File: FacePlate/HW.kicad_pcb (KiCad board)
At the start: 2 copper layers, 8 parts, among them J1 Left, J2 Audio In, J3 Audio Out, J4 Right

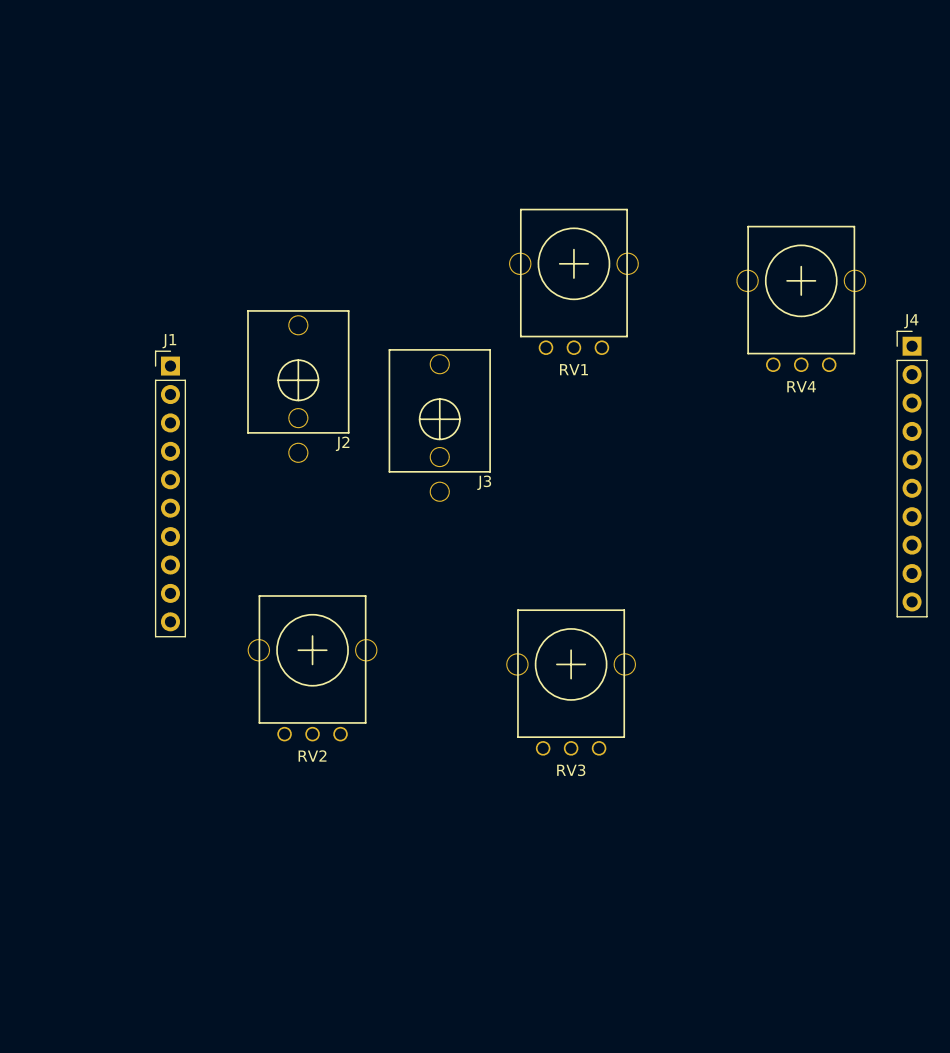
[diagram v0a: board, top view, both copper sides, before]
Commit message: Finished the IO module
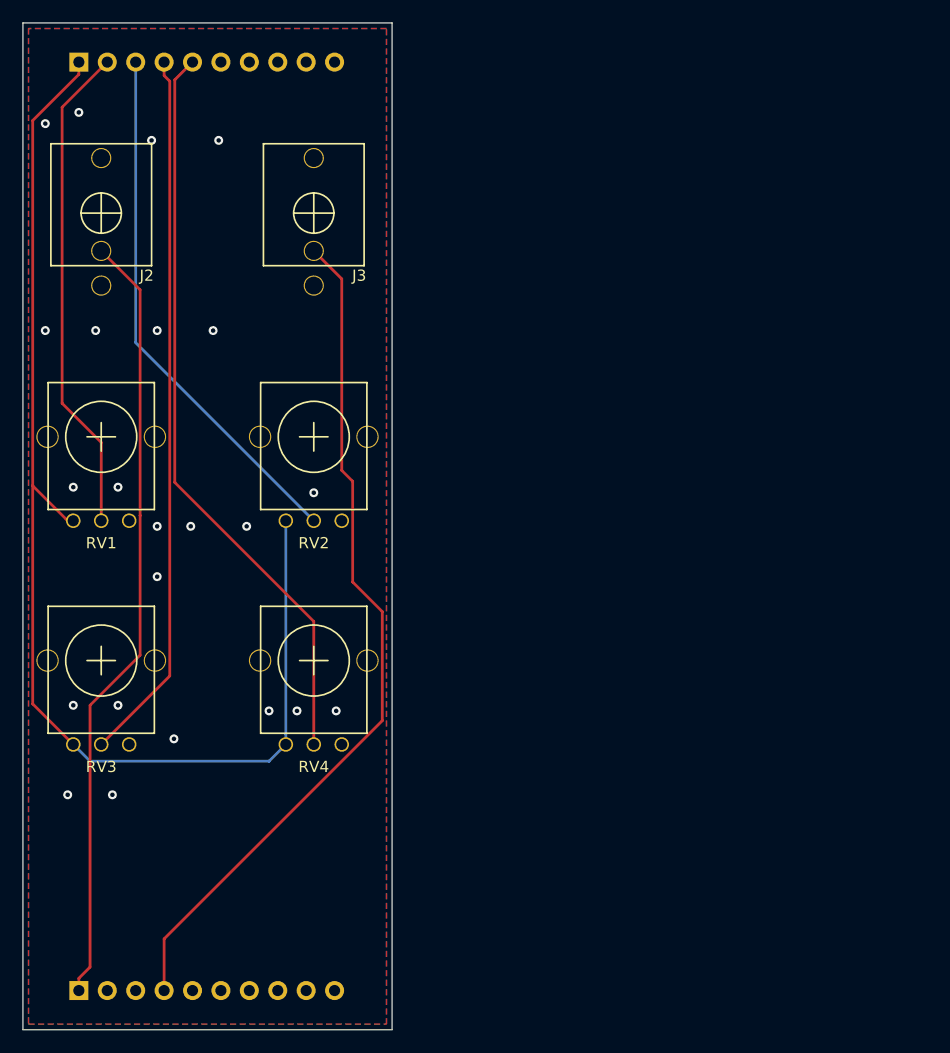
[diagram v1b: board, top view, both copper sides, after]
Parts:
- J1, J4: moved to B.Cu
- moved J4 78.7 mm to (115.0, 63.5), turned to 270 degrees
- moved J1 56.4 mm to (115.0, 146.5), turned to 270 degrees
- moved RV4 55.2 mm to (136.0, 117.0)
- moved RV1 45.0 mm to (117.0, 97.0)
- moved RV3 42.0 mm to (117.0, 117.0)
- moved J2 23.1 mm to (117.0, 77.0)
- moved J3 21.6 mm to (136.0, 77.0)
- moved RV2 19.1 mm to (136.0, 97.0)
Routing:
- net +3V3: track 0.00 -> 109.6 mm
- net /AOUT0: track 0.00 -> 76.7 mm
- net /AIN0: track 0.00 -> 69.8 mm
- net /POT3: track 0.00 -> 66.8 mm
- net /POT2: track 0.00 -> 63.7 mm
- net /POT1: track 0.00 -> 47.6 mm
- net /POT0: track 0.00 -> 44.1 mm
- net GND: vias 0 -> 23
- added copper zone on B.Cu, net GND
- added copper zone on F.Cu, net GND
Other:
- board outline added: 33 x 90 mm
